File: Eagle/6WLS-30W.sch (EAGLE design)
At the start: 36 parts, among them J1 12VDC-8A, SW1 SPDTTHRU, U1 DCDCMULT6, U2 DCDCMULT6, U3 DCDCMULT6

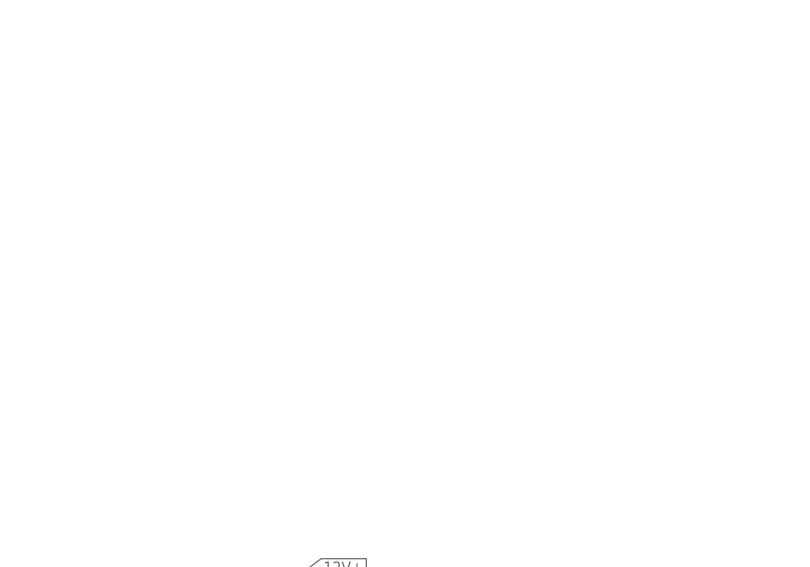
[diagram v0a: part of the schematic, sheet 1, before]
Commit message: Larger copper pads for supply pins.
Switch to larger, oblong pads for supply pins. Thanks to Prism Circuits.
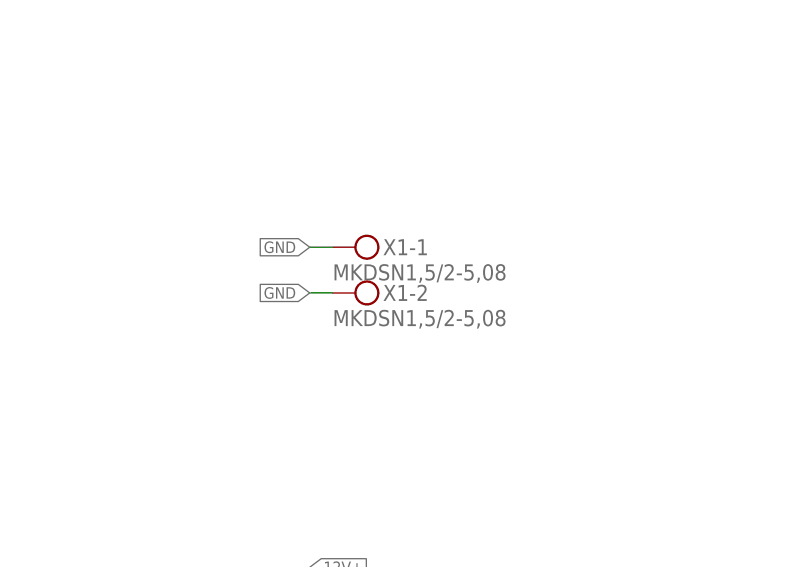
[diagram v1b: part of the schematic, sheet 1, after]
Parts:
- added X1: MKDSN1,5/2-5,08, con-phoenix-508:MKDSN1,5/2-5,08
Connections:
- net GND: now also X1-1.KL, X1-2.KL
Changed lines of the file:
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@@
 <part name="SW1" library="studio_h" deviceset="SPDT" device="THRU"/>
 <part name="SV1" library="studio_h" deviceset="MA06-2" device="CARD"/>
+<part name="X1" library="con-phoenix-508" deviceset="MKDSN1,5/2-5,08" device=""/>
 </parts>
 <sheets>
@@
 <instance part="SW1" gate="G$1" x="218.44" y="248.92"/>
 <instance part="SV1" gate="1" x="172.72" y="220.98"/>
+<instance part="X1" gate="-1" x="60.96" y="203.2"/>
+<instance part="X1" gate="-2" x="60.96" y="198.12"/>
 </instances>
 <busses>
@@
 <junction x="53.34" y="55.88"/>
 </segment>
-</net>
+<segment>
+<wire x1="58.42" y1="203.2" x2="55.88" y2="203.2" width="0.1524" layer="91"/>
+<label x="55.88" y="203.2" size="1.27" layer="95" font="vector" ratio="12" rot="R180" xref="yes"/>
+<pinref part="X1" gate="-1" pin="KL"/>
+</segment>
+<segment>
+<wire x1="58.42" y1="198.12" x2="55.88" y2="198.12" width="0.1524" layer="91"/>
+<label x="55.88" y="198.12" size="1.27" layer="95" font="vector" ratio="12" rot="R180" xref="yes"/>
+<pinref part="X1" gate="-2" pin="KL"/>
+</segment>
+</net>
